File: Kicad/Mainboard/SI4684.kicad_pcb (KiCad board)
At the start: 2 copper layers, 100 x 68 mm, 91 parts, among them J1 DC IN, J2 Ant, J3 Headphones, J4 FRONT-PCB, J5 AUDIO, U1 MIC5504-1.8YM5, U2 LM2596T-5, U3 SI4684-A10-GM, U4 LM1117T-3.3, U5 TPA6130A2RTJTG4, U6 NE5532, X1 19.2MHz

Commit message: Add files via upload
work in progress. not finished
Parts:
- removed C13, C2: 220uF, Capacitor_THT:CP_Radial_D10.0mm_P3.50mm
- removed C24, C27, C37: 10uF, Capacitor_THT:CP_Radial_D5.0mm_P2.00mm
- removed C32, C33, C36: 10p, Capacitor_THT:C_Disc_D3.0mm_W2.0mm_P2.50mm
- removed C42, C43: 47uF, Capacitor_THT:CP_Radial_D5.0mm_P2.00mm
- removed D2: 1N5822, Diode_THT:D_DO-201_P12.70mm_Horizontal
- removed G***: LOGO, Library:VRZA
- removed J4: FRONT-PCB, Connector_IDC:IDC-Header_2x05_P2.54mm_Vertical
- removed L5: 33uH, Inductor_THT:L_Radial_D7.2mm_P3.00mm_Murata_1700
- removed L6: 22uH, Inductor_THT:L_Radial_D7.2mm_P3.00mm_Murata_1700
- removed R19: 4k7, Resistor_THT:R_Axial_DIN0207_L6.3mm_D2.5mm_P10.16mm_Horizontal
- removed R20: 3k9, Resistor_THT:R_Axial_DIN0207_L6.3mm_D2.5mm_P10.16mm_Horizontal
- removed R21, R22: 220, Resistor_THT:R_Axial_DIN0207_L6.3mm_D2.5mm_P10.16mm_Horizontal
- removed R23, R24: 100k, Resistor_THT:R_Axial_DIN0207_L6.3mm_D2.5mm_P10.16mm_Horizontal
- removed REF**: 25x25 can, Library:25x25 can
- added AE1: Antenna_Shield, Connector_Coaxial:SMA_Samtec_SMA-J-P-H-ST-EM1_EdgeMount, F.Cu at (109.5, 118.6)
- added J6: DISP RIGHT, Connector_PinHeader_2.54mm:PinHeader_1x07_P2.54mm_Vertical, B.Cu at (107.6, 83.0)
- added J7: Conn_01x02_Pin, Connector_PinHeader_2.54mm:PinHeader_1x02_P2.54mm_Vertical, B.Cu at (99.0, 80.0)
- added J8: Conn_01x02_Pin, Connector_PinHeader_2.54mm:PinHeader_1x02_P2.54mm_Vertical, F.Cu at (88.5, 92.2)
- added R27: 10k, Resistor_SMD:R_0805_2012Metric_Pad1.20x1.40mm_HandSolder, B.Cu at (92.4, 112.8)
- added R28: 10k, Resistor_SMD:R_0805_2012Metric_Pad1.20x1.40mm_HandSolder, F.Cu at (81.1, 88.3)
- added R29: 10k, Resistor_SMD:R_0805_2012Metric_Pad1.20x1.40mm_HandSolder, B.Cu at (111.7, 110.3)
- added R30: 10k, Resistor_SMD:R_0603_1608Metric_Pad0.98x0.95mm_HandSolder, F.Cu at (83.9, 100.3)
- added R31: 10k, Resistor_SMD:R_0603_1608Metric_Pad0.98x0.95mm_HandSolder, F.Cu at (84.0, 101.8)
- added R32: 10k, Resistor_SMD:R_0603_1608Metric_Pad0.98x0.95mm_HandSolder, F.Cu at (84.0, 103.4)
- added SW4: SW_Push, tp4056:SW_SPST_CK_KMS2xxGP, B.Cu at (89.1, 116.2)
- added SW5: SW_Push, tp4056:SW_SPST_CK_KMS2xxGP, B.Cu at (116.4, 90.8)
- added SW6: SW_Push, tp4056:SW_SPST_CK_KMS2xxGP, B.Cu at (116.1, 110.0)
- added U12: SIQ-02FVS3, tp4056:SW-SMD_SIQ-02FVS3_1, B.Cu at (81.7, 100.3)
- added U7: ~, tp4056:TQFN-16_L3.0-W3.0-P0.50-BL-EP1.5, F.Cu at (99.2, 87.5)
- C10, C28, C31, C9: value 10uF -> 1uF; footprint Capacitor_THT:CP_Radial_D5.0mm_P2.00mm -> Capacitor_SMD:C_0805_2012Metric_Pad1.18x1.45mm_HandSolder
- C11, C8: footprint Capacitor_THT:CP_Radial_D5.0mm_P2.00mm -> Capacitor_SMD:C_0805_2012Metric_Pad1.18x1.45mm_HandSolder
- C16: value 100uF -> 10uF; footprint Capacitor_THT:CP_Radial_D10.0mm_P3.50mm -> Capacitor_SMD:C_0805_2012Metric_Pad1.18x1.45mm_HandSolder
- C20: footprint Capacitor_THT:CP_Radial_D5.0mm_P2.00mm -> Capacitor_SMD:C_0603_1608Metric
- C22: value 10uF -> 100nF; footprint Capacitor_THT:CP_Radial_D5.0mm_P2.00mm -> Capacitor_SMD:C_0805_2012Metric_Pad1.18x1.45mm_HandSolder
- C5: footprint Capacitor_SMD:C_0603_1608Metric -> Capacitor_SMD:C_0603_1608Metric_Pad1.08x0.95mm_HandSolder
- D1: footprint Package_TO_SOT_SMD:SOT-23 -> Package_TO_SOT_SMD:SOT-23W; moved to B.Cu
- J1: value DC IN -> Conn_01x03; footprint Connector_BarrelJack:BarrelJack_Horizontal -> Connector_PinHeader_2.54mm:PinHeader_1x03_P2.54mm_Vertical; moved to B.Cu
- J2: value Ant -> Conn_01x04_Pin; footprint Connector_Coaxial:SMA_Amphenol_132134-16_Vertical -> Connector_PinHeader_2.54mm:PinHeader_1x04_P2.54mm_Vertical
- J5: value AUDIO -> DISP LEFT; footprint Library:FC68405_cinch -> Connector_PinHeader_2.54mm:PinHeader_1x07_P2.54mm_Vertical; moved to B.Cu
- L1, L3, L4: footprint Inductor_SMD:L_0603_1608Metric -> Inductor_SMD:L_0603_1608Metric_Pad1.05x0.95mm_HandSolder
- R12: value 39k -> 2k; footprint Resistor_THT:R_Axial_DIN0207_L6.3mm_D2.5mm_P10.16mm_Horizontal -> Resistor_SMD:R_0603_1608Metric
- R13: value 100k -> 2k; footprint Resistor_THT:R_Axial_DIN0207_L6.3mm_D2.5mm_P10.16mm_Horizontal -> Resistor_SMD:R_0603_1608Metric
- R14: value 100k -> 3k; footprint Resistor_THT:R_Axial_DIN0207_L6.3mm_D2.5mm_P10.16mm_Horizontal -> Resistor_SMD:R_0805_2012Metric_Pad1.20x1.40mm_HandSolder
- R15: value 39k -> 100; footprint Resistor_THT:R_Axial_DIN0207_L6.3mm_D2.5mm_P10.16mm_Horizontal -> Resistor_SMD:R_0603_1608Metric
- R16: value 10 -> 0; footprint Resistor_THT:R_Axial_DIN0207_L6.3mm_D2.5mm_P10.16mm_Horizontal -> Resistor_SMD:R_0603_1608Metric
- R17: value 4k7 -> 680K; footprint Resistor_THT:R_Axial_DIN0207_L6.3mm_D2.5mm_P10.16mm_Horizontal -> Resistor_SMD:R_0805_2012Metric_Pad1.20x1.40mm_HandSolder
- R18: value 3k9 -> 0; footprint Resistor_THT:R_Axial_DIN0207_L6.3mm_D2.5mm_P10.16mm_Horizontal -> Resistor_SMD:R_0603_1608Metric
- R6: value 4k7 -> 600; footprint Resistor_THT:R_Axial_DIN0207_L6.3mm_D2.5mm_P10.16mm_Horizontal -> Resistor_SMD:R_0603_1608Metric
- R7: value 4k7 -> 100K; footprint Resistor_THT:R_Axial_DIN0207_L6.3mm_D2.5mm_P10.16mm_Horizontal -> Resistor_SMD:R_0805_2012Metric_Pad1.20x1.40mm_HandSolder
- U2: value LM2596T-5 -> BME680; footprint Package_TO_SOT_THT:TO-220-5_Vertical -> Package_LGA:Bosch_LGA-8_3x3mm_P0.8mm_ClockwisePinNumbering
- U4: value LM1117T-3.3 -> TCA9554PW; footprint Package_TO_SOT_THT:TO-220-3_Vertical -> Package_SO:TSSOP-16_4.4x5mm_P0.65mm
- U6: value NE5532 -> RT9013; footprint Package_DIP:DIP-8_W7.62mm_LongPads -> Package_TO_SOT_SMD:SOT-23-5
- moved U4 114.2 mm to (83.9, 96.8), turned to 0 degrees
- moved U2 113.6 mm to (83.8, 106.1), turned to 0 degrees
- moved J1 91.1 mm to (96.8, 96.6), turned to -90 degrees
- moved J5 85.3 mm to (92.1, 83.0)
- moved R18 82.0 mm to (82.5, 75.7), turned to 180 degrees
- moved C22 80.2 mm to (102.7, 85.1), turned to 90 degrees
- moved R16 73.2 mm to (82.5, 73.9), turned to 0 degrees
- moved C16 68.6 mm to (104.8, 85.1), turned to 90 degrees
- moved U6 63.0 mm to (89.6, 107.6), turned to 0 degrees
- moved R7 60.0 mm to (100.8, 91.5), turned to 180 degrees
- moved C28 57.5 mm to (89.7, 104.3), turned to 180 degrees
- moved J2 55.2 mm to (95.8, 83.0)
- moved R15 54.4 mm to (89.3, 96.9), turned to 180 degrees
- moved R17 54.1 mm to (103.5, 89.4), turned to 180 degrees
- moved R12 49.1 mm to (107.7, 104.1)
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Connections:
- C28 pad 1: Net-(C28-Pad1) -> GND
- C28 pad 2: L -> +5V
- C3 pad 1: Net-(J2-In) -> Net-(AE1-A)
- C31 pad 1: Net-(U6C-V+) -> GND
- C31 pad 2: GND -> +3V3
- D1 pad 3: Net-(J2-In) -> Net-(AE1-A)
- J1 pad 1: +12V -> I2SLRC
- J1 pad 2: GND -> I2SCLK
- J1 pad 3: GND -> I2SDIN
- J2 pad 1: Net-(J2-In) -> A
- J2 pad 2: GND -> B
- J5 pad 1: Net-(J5-IN1) -> RST
- J5 pad 2: Net-(J5-IN2) -> LCD_CS
- J5 pad 3: GND -> SS
- R12 pad 1: GND -> Net-(U3-DSF)
- R12 pad 2: Net-(C37-Pad1) -> I2SLRC
- R13 pad 1: Net-(U6A-+) -> Net-(U3-DCLK)
- R13 pad 2: Net-(C37-Pad1) -> I2SCLK
- R14 pad 1: Net-(C37-Pad1) -> I2SD
- R14 pad 2: Net-(U6B-+) -> Net-(U7-SD)
- R15 pad 1: Net-(C37-Pad1) -> INT
- R15 pad 2: +5V -> Net-(U4-~{INT})
- R16 pad 1: +12V -> +3V3
- R16 pad 2: Net-(U6C-V+) -> A
- R17 pad 1: Net-(U6A--) -> Net-(U7-SD)
- R17 pad 2: Net-(R17-Pad2) -> +5V
- R18 pad 1: Net-(U6A--) -> GND
- R18 pad 2: GND -> B
- R6 pad 1: Net-(C28-Pad1) -> Net-(U3-DOUT)
- R6 pad 2: Net-(U6B-+) -> I2SDIN
- R7 pad 1: Net-(C27-Pad1) -> GND
- R7 pad 2: Net-(U6A-+) -> Net-(U7-GAIN)
- U2 pad 1: +12V -> unconnected-(U2-GND-Pad1)
- U2 pad 2: Net-(D2-K) -> unconnected-(U2-CSB-Pad2)
- U2 pad 3: GND -> unconnected-(U2-SDI-Pad3)
- U2 pad 4: Net-(U2-FB) -> unconnected-(U2-SCK-Pad4)
- U2 pad 5: GND -> unconnected-(U2-SDO-Pad5)
- U3 pad 27: unconnected-(U3-DCLK-Pad27) -> Net-(U3-DCLK)
- U3 pad 28: unconnected-(U3-DSF-Pad28) -> Net-(U3-DSF)
- U3 pad 33: unconnected-(U3-DOUT-Pad33) -> Net-(U3-DOUT)
- U4 pad 2: +3V3 -> GND
- U4 pad 3: +5V -> GND
- U6 pad 1: Net-(R17-Pad2) -> +5V
- U6 pad 2: Net-(U6A--) -> GND
- U6 pad 3: Net-(U6A-+) -> +5V
- U6 pad 4: GND -> unconnected-(U6-FB-Pad4)
- U6 pad 5: Net-(U6B-+) -> +3V3
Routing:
- net +3V3: track 235.6 -> 35.5 mm
- net R: track 134.2 -> 14.5 mm
- net +12V: track 98.7 -> 0.00 mm
- net L: track 80.8 -> 0.00 mm
- net Net-(U2-FB): track 52.4 -> 0.00 mm
- net +5V: track 101.4 -> 49.9 mm, vias 0 -> 1
- net Net-(J5-IN2): track 29.0 -> 0.00 mm
- net Net-(R19-Pad2): track 28.4 -> 0.00 mm
- net INT: track 34.2 -> 7.36 mm, vias 3 -> 0
- net RST: track 30.5 -> 3.91 mm, vias 3 -> 0
- net Net-(U6A-+): track 25.4 -> 0.00 mm
- net Net-(U6C-V+): track 25.2 -> 0.00 mm
- net I2SLRC: track 0.00 -> 25.1 mm, vias 0 -> 1
- net +1V8: track 57.6 -> 32.7 mm
- net Net-(J5-IN1): track 24.3 -> 0.00 mm
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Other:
- board size 100 x 68 mm -> 41.6 x 42.2 mm
- board text removed: "Bouwproject 2024"
- board text removed: "PE5PVB"
- board text removed: "Radiokampweek"
- board text removed: "SI4684 receiver"

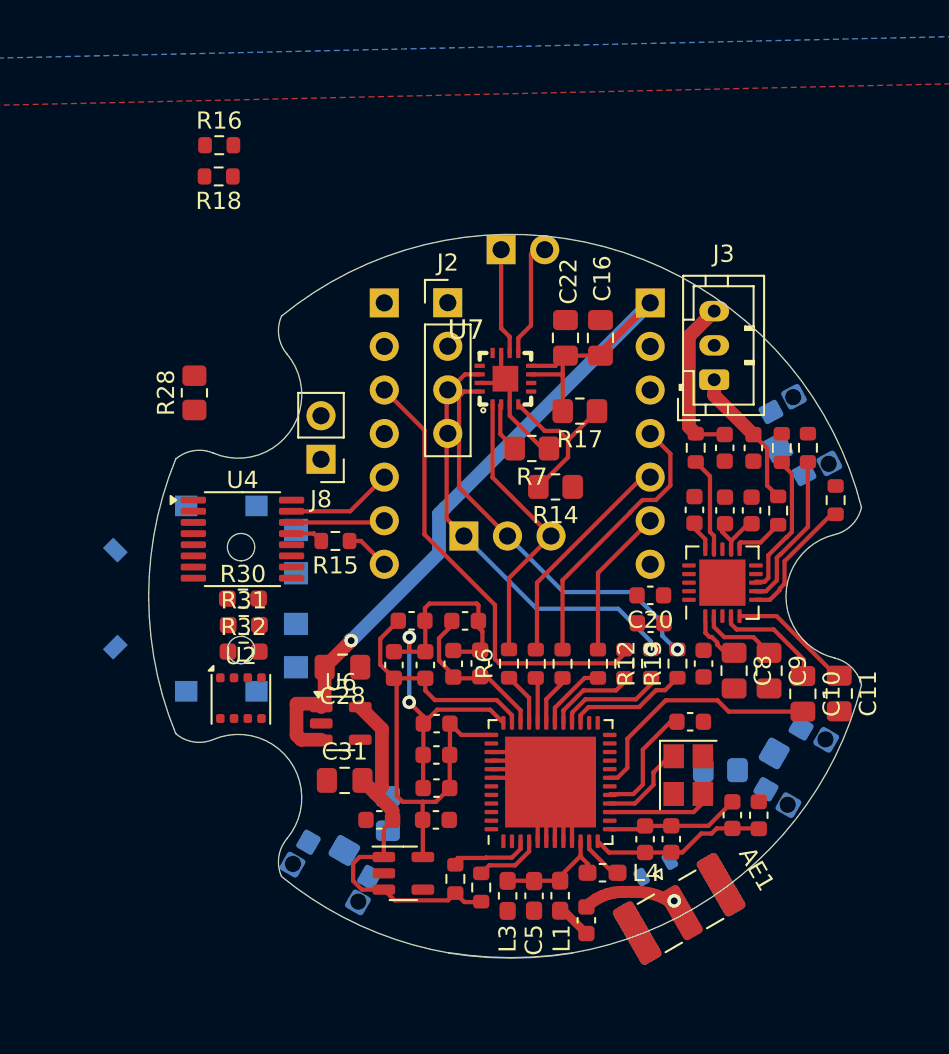
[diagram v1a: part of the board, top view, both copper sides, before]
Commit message: Add files via upload
fixed some layout issues. still work in progress
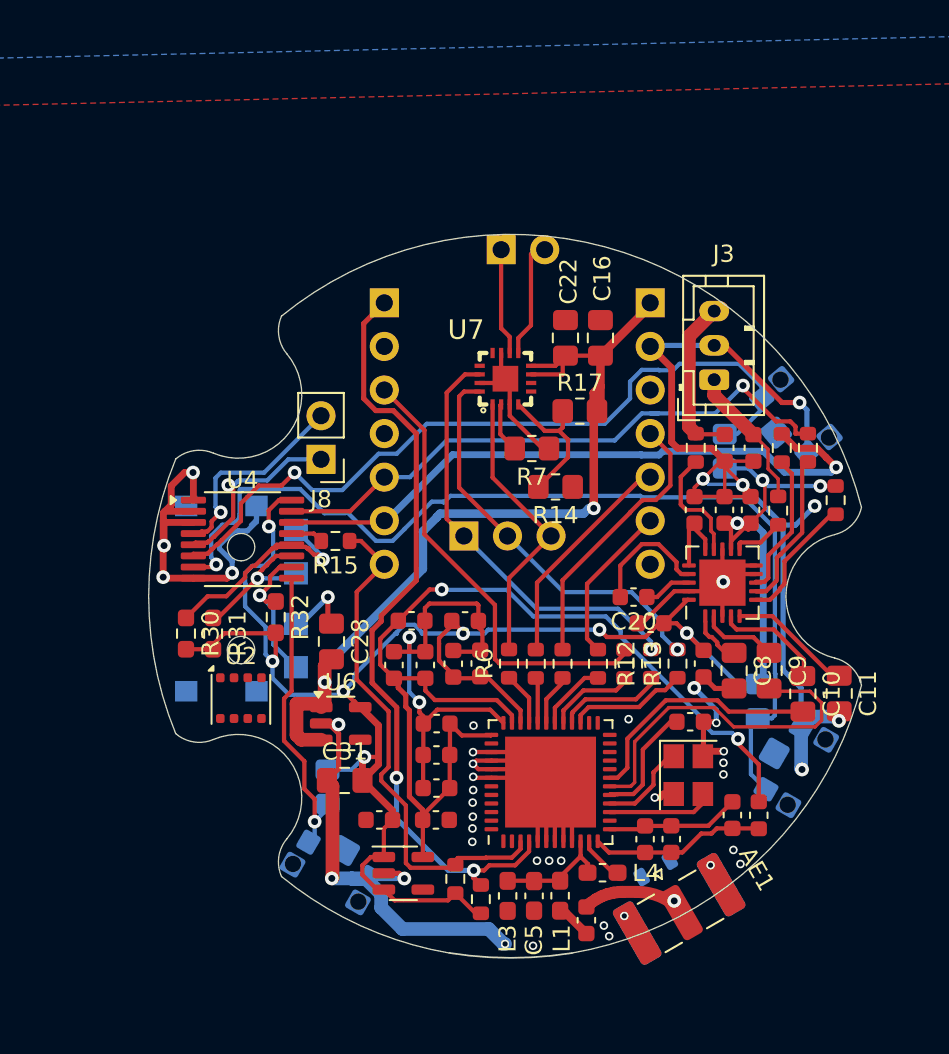
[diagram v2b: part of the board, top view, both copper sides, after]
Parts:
- removed J2: Conn_01x04_Pin, Connector_PinHeader_2.54mm:PinHeader_1x04_P2.54mm_Vertical
- removed R16, R18: 0, Resistor_SMD:R_0603_1608Metric
- R28: moved to B.Cu
- moved R28 31.1 mm to (112.0, 91.7)
- moved R29 4.57 mm to (113.9, 106.3), turned to 90 degrees
- moved R30 3.90 mm to (80.6, 102.3), turned to -90 degrees
- moved R27 3.85 mm to (88.8, 111.3)
- moved R32 2.75 mm to (85.8, 101.4), turned to -90 degrees
- moved R31 1.86 mm to (82.2, 102.3), turned to -90 degrees
- moved C28 1.63 mm to (89.1, 102.8), turned to -90 degrees
- moved SW5 1.17 mm to (116.1, 89.7), turned to -50 degrees
- moved C20 0.98 mm to (106.7, 100.2)
- moved R25 0.68 mm to (97.8, 117.8)
- moved C15 0.07 mm to (113.5, 95.1)
- turned R17 to 0 degrees
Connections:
- J8 pad 1: P3 -> P1
- J8 pad 2: P2 -> P0
- R27 pad 2: SWITCH2 -> P4
- R28 pad 2: SWITCH1 -> P2
- R29 pad 1: SWITCH3 -> P3
- SW4 pad 1: SWITCH2 -> GND
- SW4 pad 2: GND -> P4
- SW5 pad 1: GND -> P2
- SW5 pad 2: SWITCH1 -> GND
- SW6 pad 2: SWITCH3 -> P3
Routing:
- net GND: track 30.9 -> 178.4 mm, vias 0 -> 42
- net +3V3: track 35.5 -> 121.4 mm, vias 0 -> 10
- net P3: track 0.00 -> 58.5 mm, vias 0 -> 1
- net P2: track 0.00 -> 43.8 mm, vias 0 -> 1
- net RST: track 3.91 -> 45.2 mm, vias 0 -> 2
- net SCL: track 5.45 -> 38.1 mm, vias 0 -> 1
- net SDA: track 6.23 -> 35.3 mm, vias 0 -> 1
- net +1V8: track 32.7 -> 61.5 mm, vias 0 -> 2
- net INT: track 7.36 -> 30.1 mm
- net L: track 0.00 -> 20.7 mm
- net P4: track 0.00 -> 17.8 mm, vias 0 -> 1
- net P7: track 0.00 -> 13.7 mm, vias 0 -> 1
- net P0: track 0.00 -> 12.1 mm, vias 0 -> 1
- net P1: track 0.00 -> 11.0 mm, vias 0 -> 1
- net P5: track 0.00 -> 9.07 mm, vias 0 -> 1
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
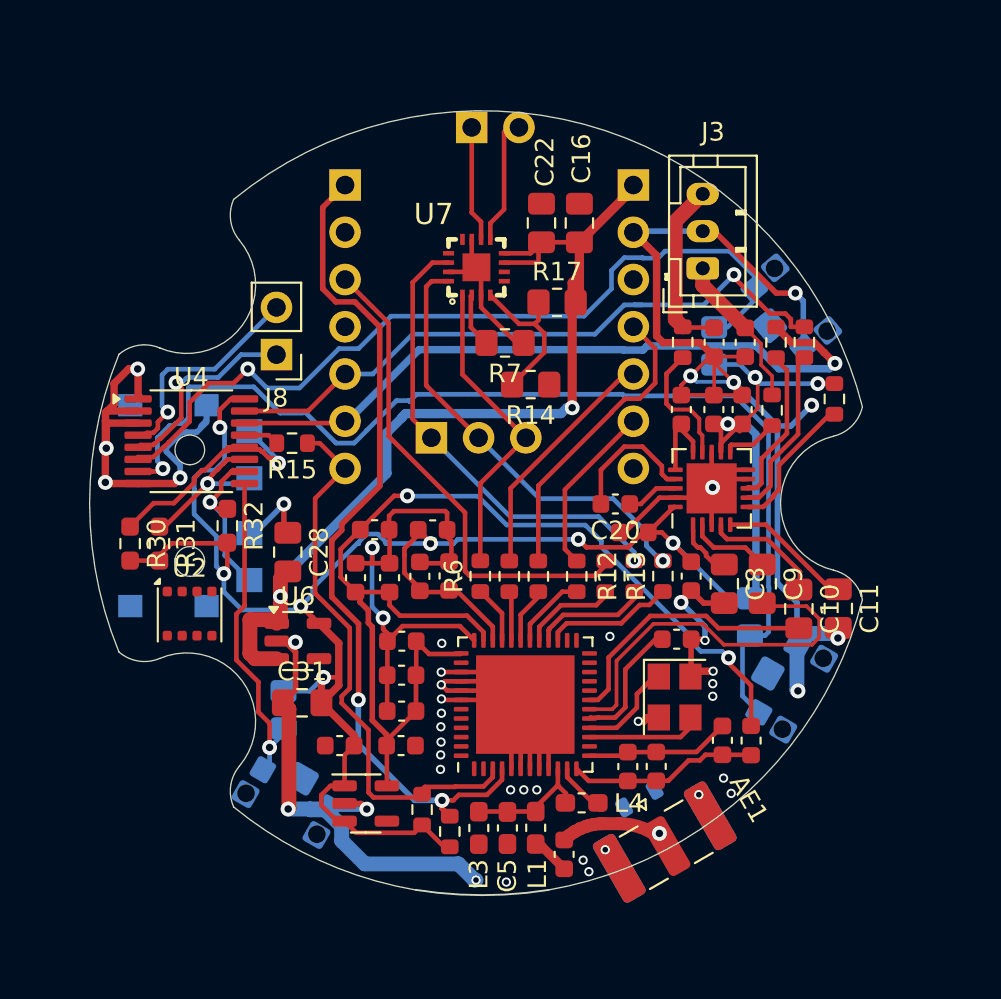
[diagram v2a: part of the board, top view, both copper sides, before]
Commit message: Add files via upload
added Display connector
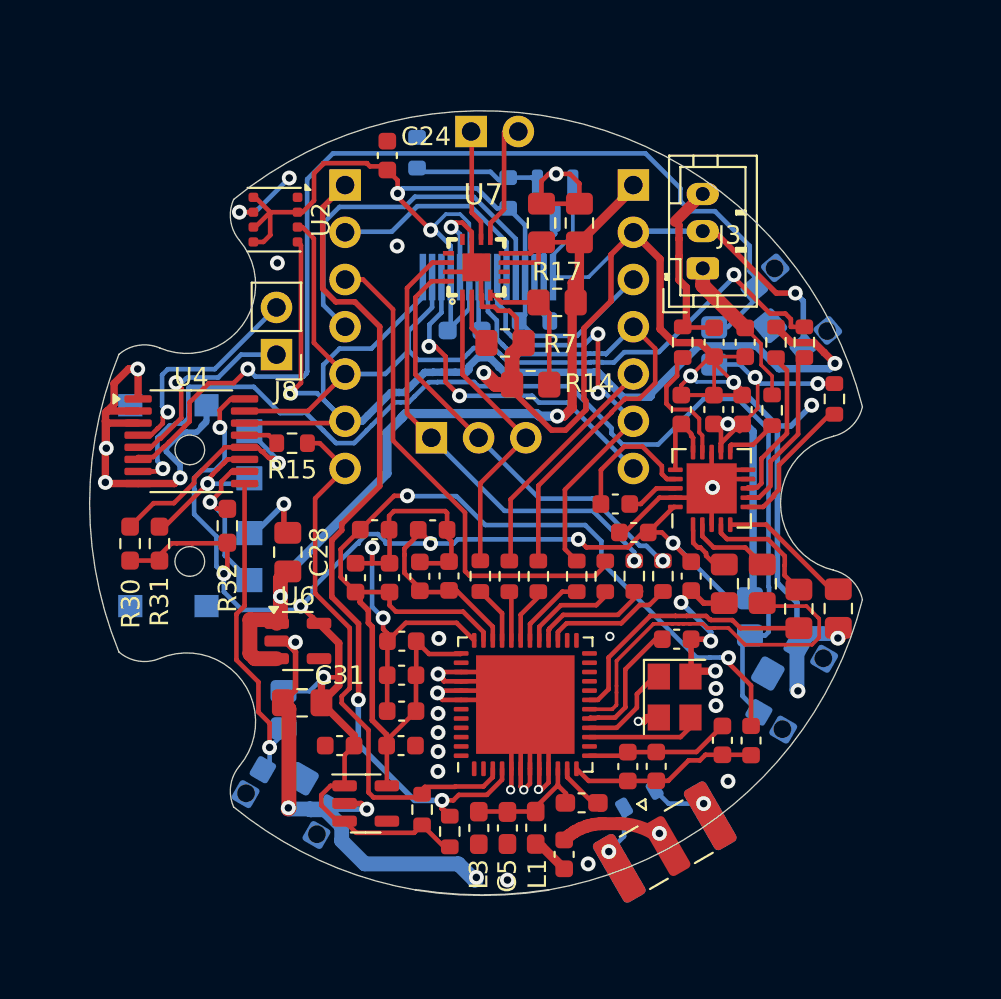
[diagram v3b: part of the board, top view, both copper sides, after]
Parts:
- added C24: 100n, Capacitor_SMD:C_0603_1608Metric, F.Cu at (94.4, 81.5)
- added Q2: 2N7002, Package_TO_SOT_SMD:SOT-23, B.Cu at (103.4, 83.9)
- added R18: 10k, Resistor_SMD:R_0603_1608Metric, B.Cu at (100.9, 83.5)
- added R19: 1M, Resistor_SMD:R_0603_1608Metric, B.Cu at (96.0, 81.3)
- added R22: 22, Resistor_SMD:R_0603_1608Metric, B.Cu at (102.3, 90.4)
- added R34: 10k, Resistor_SMD:R_0603_1608Metric_Pad0.98x0.95mm_HandSolder, B.Cu at (98.6, 90.9)
- added U13: ~, open-Smartwatch:GC9A01_Touch_IPS_display_reversed_16pin, B.Cu at (99.5, 87.8)
- moved U2 21.7 mm to (88.4, 84.9), turned to -90 degrees
- moved J7 0.22 mm to (98.9, 80.2)
- turned R14 to 0 degrees
- renumbered AE1 to ANT1
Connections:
- J6 pad 7: unconnected-(J6-Pin_7-Pad7) -> TP2_INT
- R14 pad 1: I2SD -> GND
- U2 pad 1: unconnected-(U2-GND-Pad1) -> GND
- U2 pad 2: unconnected-(U2-CSB-Pad2) -> +3.3VA
- U2 pad 3: unconnected-(U2-SDI-Pad3) -> SDA
- U2 pad 4: unconnected-(U2-SCK-Pad4) -> SCL
- U2 pad 5: unconnected-(U2-SDO-Pad5) -> +3.3VA
- U2 pad 6: unconnected-(U2-VDDIO-Pad6) -> +3.3VA
- U2 pad 7: unconnected-(U2-GND-Pad7) -> GND
- U2 pad 8: unconnected-(U2-VDD-Pad8) -> +3.3VA
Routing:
- net GND: track 178.4 -> 239.3 mm, vias 42 -> 45
- net +3.3VA: track 0.00 -> 53.3 mm, vias 0 -> 2
- net SCL: track 38.1 -> 63.8 mm, vias 1 -> 2
- net LCD_DC: track 0.00 -> 20.6 mm
- net TP2_INT: track 0.00 -> 18.5 mm, vias 0 -> 2
- net CLK: track 9.30 -> 23.9 mm, vias 0 -> 2
- net SDA: track 35.3 -> 49.6 mm
- net LCD_CS: track 0.00 -> 12.0 mm
- net MOSI: track 16.1 -> 28.0 mm
- net P2: track 43.8 -> 54.4 mm
- net Net-(Q2-G): track 0.00 -> 6.50 mm
- net /LEDK: track 0.00 -> 3.43 mm
- net Net-(U13-RST): track 0.00 -> 2.89 mm
- net P3: track 58.5 -> 61.2 mm
- net Net-(U13-LEDA): track 0.00 -> 2.70 mm
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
